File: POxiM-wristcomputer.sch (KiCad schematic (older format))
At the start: 8 parts

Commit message: schematic donish
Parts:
- removed R? (x2): R_Small, symbol Device:R_Small
- J1: renamed from J?; footprint (none) -> POxiM-uncategorised:Micro-B_Molex_105017-0001; Mfr. (none) -> Molex; Mfr. No. (none) -> 105017-0001; Mouser No. (none) -> 538-105017-0001
- J2: renamed from J?; footprint (none) -> POxiM-uncategorised:CUI_SJ-43514-SMT; Mfr. (none) -> CUI Devices; Mfr. No. (none) -> SJ-43514-SMT-TR; Mouser No. (none) -> 490-SJ-43514-SMT-TR
- gave numbers to parts that had none: 4
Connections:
- wire segments 30 -> 35
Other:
- note added: "for audio:\nmic\ngnd\nright\nleft\n"
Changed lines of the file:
@@
 F1 "Subschematics/SignalConditioning.sch" 50
 F2 "LEDDrive.IR" I L 8200 3700 50
-F3 "LEDOut.IR" O R 9850 3600 50
+F3 "LEDOut.IR" O R 9850 3800 50
 F4 "LEDDrive.Red" I L 8200 3600 50
-F5 "LEDOut.Red" O R 9850 3700 50
+F5 "LEDOut.Red" O R 9850 3900 50
 F6 "GND" I L 8200 4400 50
 F7 "PhotoDiodeInternal" O L 8200 4200 50
-F8 "PhotoDiode" I R 9850 3800 50
-F9 "+5V" I L 8200 3300 50
+F8 "PhotoDiode" I R 9850 3600 50
 $EndSheet
 $Comp
-L Connector:AudioJack4_Ground J?
+L Connector:AudioJack4_Ground J2
 U 1 1 5EBC41F5
 P 10500 3700
-F 0 "J?" H 10170 3618 50  0000 R CNN
+F 0 "J2" H 10170 3618 50  0000 R CNN
 F 1 "AudioJack4_Ground" H 10170 3527 50  0000 R CNN
-F 2 "" H 10500 3700 50  0001 C CNN
-F 3 "~" H 10500 3700 50  0001 C CNN
+F 2 "POxiM-uncategorised:CUI_SJ-43514-SMT" H 10500 3700 50  0001 C CNN
+F 3 "https://nl.mouser.com/datasheet/2/670/sj-4351x-smt-1779337.pdf" H 10500 3700 50  0001 C CNN
+F 4 "CUI Devices" H 10500 3700 50  0001 C CNN "Mfr."
+F 5 "SJ-43514-SMT-TR" H 10500 3700 50  0001 C CNN "Mfr. No."
+F 6 "490-SJ-43514-SMT-TR" H 10500 3700 50  0001 C CNN "Mouser No."
 	1    10500 3700
 	-1   0    0    -1
@@
 F6 "ADC_feedback" O R 5750 4250 50
 F7 "ADC_input" I R 5750 4150 50
-F8 "SWIM" O L 4100 3500 50
+F8 "SWIM" O L 4100 3650 50
 F9 "LED_R" O R 5750 3600 50
 F10 "LED_IR" O R 5750 3700 50
-F11 "UART1_TX" O L 4100 3600 50
+F11 "UART1_TX" O L 4100 3800 50
 $EndSheet
 $Sheet
@@
 F0 "USB interface" 50
 F1 "Subschematics/USB.sch" 50
+F2 "5V_input" I L 2150 3500 50
+F3 "5V_protected" O R 3800 3250 50
+F4 "Data+" O L 2150 3700 50
+F5 "Data-" O L 2150 3800 50
+F6 "GND" I L 2150 4450 50
+F7 "SWIM" I R 3800 3650 50
+F8 "DataTX" I R 3800 3800 50
 $EndSheet
 $Comp
-L Connector:USB_B_Micro J?
+L Connector:USB_B_Micro J1
 U 1 1 5EBC5F66
 P 950 3700
-F 0 "J?" H 1007 4167 50  0000 C CNN
+F 0 "J1" H 1007 4167 50  0000 C CNN
 F 1 "USB_B_Micro" H 1007 4076 50  0000 C CNN
-F 2 "" H 1100 3650 50  0001 C CNN
+F 2 "POxiM-uncategorised:Micro-B_Molex_105017-0001" H 1100 3650 50  0001 C CNN
 F 3 "~" H 1100 3650 50  0001 C CNN
+F 4 "Molex" H 950 3700 50  0001 C CNN "Mfr."
+F 5 "105017-0001" H 950 3700 50  0001 C CNN "Mfr. No."
+F 6 "538-105017-0001" H 950 3700 50  0001 C CNN "Mouser No."
 	1    950  3700
 	1    0    0    -1
@@
 	7550 2300 7400 2300
 $Comp
-L Mechanical:MountingHole H?
+L Mechanical:MountingHole H4
 U 1 1 5EDAD0C3
 P 1750 7400
-F 0 "H?" H 1850 7446 50  0000 L CNN
+F 0 "H4" H 1850 7446 50  0000 L CNN
 F 1 "MountingHole" H 1850 7355 50  0000 L CNN
 F 2 "MountingHole:MountingHole_2.2mm_M2_DIN965" H 1750 7400 50  0001 C CNN
 F 3 "~" H 1750 7400 50  0001 C CNN
+F 4 "~" H 1750 7400 50  0001 C CNN "Mfr."
+F 5 "~" H 1750 7400 50  0001 C CNN "Mfr. No."
+F 6 "~" H 1750 7400 50  0001 C CNN "Mouser No."
 	1    1750 7400
 	1    0    0    -1
 $EndComp
 $Comp
-L Mechanical:MountingHole H?
+L Mechanical:MountingHole H3
 U 1 1 5EDAD9CE
 P 1750 7100
-F 0 "H?" H 1850 7146 50  0000 L CNN
+F 0 "H3" H 1850 7146 50  0000 L CNN
 F 1 "MountingHole" H 1850 7055 50  0000 L CNN
 F 2 "MountingHole:MountingHole_2.2mm_M2_DIN965" H 1750 7100 50  0001 C CNN
 F 3 "~" H 1750 7100 50  0001 C CNN
+F 4 "~" H 1750 7100 50  0001 C CNN "Mfr."
+F 5 "~" H 1750 7100 50  0001 C CNN "Mfr. No."
+F 6 "~" H 1750 7100 50  0001 C CNN "Mouser No."
 	1    1750 7100
 	1    0    0    -1
 $EndComp
 $Comp
-L Mechanical:MountingHole H?
+L Mechanical:MountingHole H1
 U 1 1 5EDAE2DB
 P 900 7100
-F 0 "H?" H 1000 7146 50  0000 L CNN
+F 0 "H1" H 1000 7146 50  0000 L CNN
 F 1 "MountingHole" H 1000 7055 50  0000 L CNN
 F 2 "MountingHole:MountingHole_2.2mm_M2_DIN965" H 900 7100 50  0001 C CNN
 F 3 "~" H 900 7100 50  0001 C CNN
+F 4 "~" H 900 7100 50  0001 C CNN "Mfr."
+F 5 "~" H 900 7100 50  0001 C CNN "Mfr. No."
+F 6 "~" H 900 7100 50  0001 C CNN "Mouser No."
 	1    900  7100
 	1    0    0    -1
 $EndComp
 $Comp
-L Mechanical:MountingHole H?
+L Mechanical:MountingHole H2
 U 1 1 5EDAE92A
 P 900 7400
-F 0 "H?" H 1000 7446 50  0000 L CNN
+F 0 "H2" H 1000 7446 50  0000 L CNN
 F 1 "MountingHole" H 1000 7355 50  0000 L CNN
 F 2 "MountingHole:MountingHole_2.2mm_M2_DIN965" H 900 7400 50  0001 C CNN
 F 3 "~" H 900 7400 50  0001 C CNN
+F 4 "~" H 900 7400 50  0001 C CNN "Mfr."
+F 5 "~" H 900 7400 50  0001 C CNN "Mfr. No."
+F 6 "~" H 900 7400 50  0001 C CNN "Mouser No."
 	1    900  7400
 	1    0    0    -1
@@
 Connection ~ 950  4200
 $Comp
-L power:GND #PWR?
+L power:GND #PWR01
 U 1 1 5EDB1CEA
 P 950 4300
-F 0 "#PWR?" H 950 4050 50  0001 C CNN
+F 0 "#PWR01" H 950 4050 50  0001 C CNN
 F 1 "GND" H 955 4127 50  0000 C CNN
 F 2 "" H 950 4300 50  0001 C CNN
@@
 	1    0    0    -1
 $EndComp
-Wire Wire Line
-	1250 3500 2000 3500
 Text Label 1900 3500 2    50   ~ 0
 5V_power_input
-Wire Wire Line
-	1250 3800 1450 3800
-Wire Wire Line
-	1250 3700 1450 3700
 NoConn ~ 1250 3900
 Wire Wire Line
 	10300 3800 9850 3800
 Wire Wire Line
-	10300 3700 9850 3700
+	10300 3700 10250 3700
 Wire Wire Line
 	9850 3600 10300 3600
 Wire Wire Line
-	10300 3900 10250 3900
-Wire Wire Line
-	10250 3900 10250 4200
-Wire Wire Line
 	10500 4100 10500 4200
 Wire Wire Line
 	10500 4200 10250 4200
-Connection ~ 10250 4200
 Wire Wire Line
 	10250 4200 10250 4750
@@
 	8100 4400 8100 4800
 $Comp
-L power:GND #PWR?
+L power:GND #PWR07
 U 1 1 5EDBAF1B
 P 8100 4800
-F 0 "#PWR?" H 8100 4550 50  0001 C CNN
+F 0 "#PWR07" H 8100 4550 50  0001 C CNN
 F 1 "GND" H 8105 4627 50  0000 C CNN
 F 2 "" H 8100 4800 50  0001 C CNN
@@
 $EndComp
 $Comp
-L power:GND #PWR?
+L power:GND #PWR08
 U 1 1 5EDBAF6C
 P 10250 4750
-F 0 "#PWR?" H 10250 4500 50  0001 C CNN
+F 0 "#PWR08" H 10250 4500 50  0001 C CNN
 F 1 "GND" H 10255 4577 50  0000 C CNN
 F 2 "" H 10250 4750 50  0001 C CNN
@@
 	5750 3600 8200 3600
 Wire Wire Line
-	8200 3300 8000 3300
-Wire Wire Line
-	8000 3300 8000 3100
-$Comp
-L power:+5V #PWR?
-U 1 1 5EDBE13D
-P 8000 3100
-F 0 "#PWR?" H 8000 2950 50  0001 C CNN
-F 1 "+5V" H 8015 3273 50  0000 C CNN
-F 2 "" H 8000 3100 50  0001 C CNN
-F 3 "" H 8000 3100 50  0001 C CNN
-	1    8000 3100
-	1    0    0    -1
-$EndComp
-Wire Wire Line
 	5750 3700 8200 3700
 Wire Wire Line
@@
 	6150 4400 6150 4550
 $Comp
-L power:+5V #PWR?
+L power:+5V #PWR05
 U 1 1 5EDBFF74
 P 6150 3950
-F 0 "#PWR?" H 6150 3800 50  0001 C CNN
+F 0 "#PWR05" H 6150 3800 50  0001 C CNN
 F 1 "+5V" H 6165 4123 50  0000 C CNN
 F 2 "" H 6150 3950 50  0001 C CNN
@@
 $EndComp
 $Comp
-L power:GND #PWR?
+L power:GND #PWR06
 U 1 1 5EDC0E1F
 P 6150 4550
-F 0 "#PWR?" H 6150 4300 50  0001 C CNN
+F 0 "#PWR06" H 6150 4300 50  0001 C CNN
 F 1 "GND" H 6155 4377 50  0000 C CNN
 F 2 "" H 6150 4550 50  0001 C CNN
@@
 	1    0    0    -1
 $EndComp
-$Comp
-L Device:R_Small R?
-U 1 1 5EDC2FF6
-P 1550 3700
-F 0 "R?" V 1746 3700 50  0000 C CNN
-F 1 "R_Small" V 1655 3700 50  0000 C CNN
-F 2 "" H 1550 3700 50  0001 C CNN
-F 3 "~" H 1550 3700 50  0001 C CNN
-	1    1550 3700
-	0    -1   -1   0
-$EndComp
-Wire Wire Line
-	1650 3700 2000 3700
-$Comp
-L Device:R_Small R?
-U 1 1 5EDC4868
-P 1550 3800
-F 0 "R?" V 1746 3800 50  0000 C CNN
-F 1 "R_Small" V 1655 3800 50  0000 C CNN
-F 2 "" H 1550 3800 50  0001 C CNN
-F 3 "~" H 1550 3800 50  0001 C CNN
-	1    1550 3800
-	0    -1   -1   0
-$EndComp
-Wire Wire Line
-	1650 3800 2000 3800
+Wire Wire Line
+	4100 3650 3800 3650
+Wire Wire Line
+	4100 3800 3800 3800
+Wire Wire Line
+	3800 3250 3950 3250
+Wire Wire Line
+	3950 3250 3950 2700
+Connection ~ 3950 3250
+Wire Wire Line
+	3950 3250 4100 3250
+$Comp
+L power:+5V #PWR04
+U 1 1 5EBC7CAA
+P 3950 2700
+F 0 "#PWR04" H 3950 2550 50  0001 C CNN
+F 1 "+5V" H 3965 2873 50  0000 C CNN
+F 2 "" H 3950 2700 50  0001 C CNN
+F 3 "" H 3950 2700 50  0001 C CNN
+	1    3950 2700
+	1    0    0    -1
+$EndComp
+$Comp
+L power:GND #PWR02
+U 1 1 5EBC7E84
+P 1950 4600
+F 0 "#PWR02" H 1950 4350 50  0001 C CNN
+F 1 "GND" H 1955 4427 50  0000 C CNN
+F 2 "" H 1950 4600 50  0001 C CNN
+F 3 "" H 1950 4600 50  0001 C CNN
+	1    1950 4600
+	1    0    0    -1
+$EndComp
+Wire Wire Line
+	2150 4450 1950 4450
+Wire Wire Line
+	1950 4450 1950 4600
+Wire Wire Line
+	1250 3500 2150 3500
+Wire Wire Line
+	1250 3800 2150 3800
+Wire Wire Line
+	1250 3700 2150 3700
+$Comp
+L power:GND #PWR03
+U 1 1 5EBE7B4C
+P 3900 4600
+F 0 "#PWR03" H 3900 4350 50  0001 C CNN
+F 1 "GND" H 3905 4427 50  0000 C CNN
+F 2 "" H 3900 4600 50  0001 C CNN
+F 3 "" H 3900 4600 50  0001 C CNN
+	1    3900 4600
+	1    0    0    -1
+$EndComp
+Wire Wire Line
+	4100 4450 3900 4450
+Wire Wire Line
+	3900 4450 3900 4600
+Wire Wire Line
+	10250 3700 10250 4200
+Connection ~ 10250 4200
+Wire Wire Line
+	10300 3900 9850 3900
+Text Notes 10400 3400 0    50   ~ 0
+for audio:\nmic\ngnd\nright\nleft\n
 $EndSCHEMATC

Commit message: looks real
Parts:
- removed H3, H4: MountingHole, MountingHole:MountingHole_2.2mm_M2_DIN965, symbol Mechanical:MountingHole
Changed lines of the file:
@@
 EESchema Schematic File Version 4
-LIBS:POxiM-wristcomputer-cache
-EELAYER 29 0
+EELAYER 30 0
 EELAYER END
 $Descr A4 11693 8268
@@
 	7550 2300 7400 2300
 $Comp
-L Mechanical:MountingHole H4
-U 1 1 5EDAD0C3
-P 1750 7400
-F 0 "H4" H 1850 7446 50  0000 L CNN
-F 1 "MountingHole" H 1850 7355 50  0000 L CNN
-F 2 "MountingHole:MountingHole_2.2mm_M2_DIN965" H 1750 7400 50  0001 C CNN
-F 3 "~" H 1750 7400 50  0001 C CNN
-F 4 "~" H 1750 7400 50  0001 C CNN "Mfr."
-F 5 "~" H 1750 7400 50  0001 C CNN "Mfr. No."
-F 6 "~" H 1750 7400 50  0001 C CNN "Mouser No."
-	1    1750 7400
-	1    0    0    -1
-$EndComp
-$Comp
-L Mechanical:MountingHole H3
-U 1 1 5EDAD9CE
-P 1750 7100
-F 0 "H3" H 1850 7146 50  0000 L CNN
-F 1 "MountingHole" H 1850 7055 50  0000 L CNN
-F 2 "MountingHole:MountingHole_2.2mm_M2_DIN965" H 1750 7100 50  0001 C CNN
-F 3 "~" H 1750 7100 50  0001 C CNN
-F 4 "~" H 1750 7100 50  0001 C CNN "Mfr."
-F 5 "~" H 1750 7100 50  0001 C CNN "Mfr. No."
-F 6 "~" H 1750 7100 50  0001 C CNN "Mouser No."
-	1    1750 7100
-	1    0    0    -1
-$EndComp
-$Comp
 L Mechanical:MountingHole H1

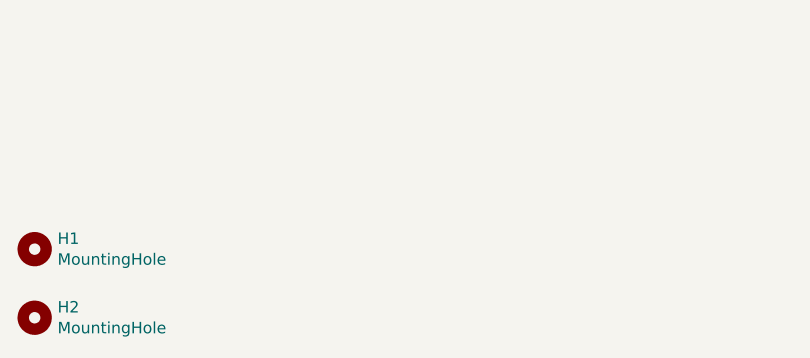
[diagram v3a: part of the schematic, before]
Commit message: Refactor based on feedback from Daniel
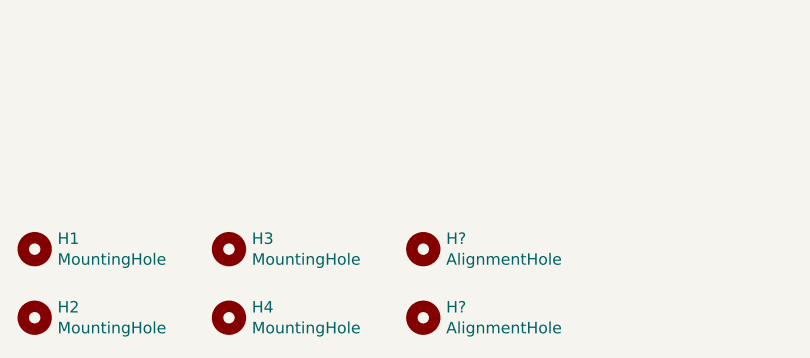
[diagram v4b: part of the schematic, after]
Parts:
- added H3, H4: MountingHole, MountingHole:MountingHole_2.2mm_M2_DIN965, symbol Mechanical:MountingHole
- added H? (x2): AlignmentHole, MountingHole:MountingHole_2.2mm_M2_DIN965, symbol Mechanical:MountingHole
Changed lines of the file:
@@
 EESchema Schematic File Version 4
-EELAYER 30 0
+LIBS:POxiM-wristcomputer-cache
+EELAYER 29 0
 EELAYER END
 $Descr A4 11693 8268
@@
 Text Notes 10400 3400 0    50   ~ 0
 for audio:\nmic\ngnd\nright\nleft\n
+$Comp
+L Mechanical:MountingHole H3
+U 1 1 5EBE9DDE
+P 1750 7100
+F 0 "H3" H 1850 7146 50  0000 L CNN
+F 1 "MountingHole" H 1850 7055 50  0000 L CNN
+F 2 "MountingHole:MountingHole_2.2mm_M2_DIN965" H 1750 7100 50  0001 C CNN
+F 3 "~" H 1750 7100 50  0001 C CNN
+F 4 "~" H 1750 7100 50  0001 C CNN "Mfr."
+F 5 "~" H 1750 7100 50  0001 C CNN "Mfr. No."
+F 6 "~" H 1750 7100 50  0001 C CNN "Mouser No."
+	1    1750 7100
+	1    0    0    -1
+$EndComp
+$Comp
+L Mechanical:MountingHole H4
+U 1 1 5EBE9DE7
+P 1750 7400
+F 0 "H4" H 1850 7446 50  0000 L CNN
+F 1 "MountingHole" H 1850 7355 50  0000 L CNN
+F 2 "MountingHole:MountingHole_2.2mm_M2_DIN965" H 1750 7400 50  0001 C CNN
+F 3 "~" H 1750 7400 50  0001 C CNN
+F 4 "~" H 1750 7400 50  0001 C CNN "Mfr."
+F 5 "~" H 1750 7400 50  0001 C CNN "Mfr. No."
+F 6 "~" H 1750 7400 50  0001 C CNN "Mouser No."
+	1    1750 7400
+	1    0    0    -1
+$EndComp
+$Comp
+L Mechanical:MountingHole H?
+U 1 1 5EC0DFF9
+P 2600 7100
+F 0 "H?" H 2700 7146 50  0000 L CNN
+F 1 "AlignmentHole" H 2700 7055 50  0000 L CNN
+F 2 "MountingHole:MountingHole_2.2mm_M2_DIN965" H 2600 7100 50  0001 C CNN
+F 3 "~" H 2600 7100 50  0001 C CNN
+F 4 "~" H 2600 7100 50  0001 C CNN "Mfr."
+F 5 "~" H 2600 7100 50  0001 C CNN "Mfr. No."
+F 6 "~" H 2600 7100 50  0001 C CNN "Mouser No."
+	1    2600 7100
+	1    0    0    -1
+$EndComp
+$Comp
+L Mechanical:MountingHole H?
+U 1 1 5EC0E002
+P 2600 7400
+F 0 "H?" H 2700 7446 50  0000 L CNN
+F 1 "AlignmentHole" H 2700 7355 50  0000 L CNN
+F 2 "MountingHole:MountingHole_2.2mm_M2_DIN965" H 2600 7400 50  0001 C CNN
+F 3 "~" H 2600 7400 50  0001 C CNN
+F 4 "~" H 2600 7400 50  0001 C CNN "Mfr."
+F 5 "~" H 2600 7400 50  0001 C CNN "Mfr. No."
+F 6 "~" H 2600 7400 50  0001 C CNN "Mouser No."
+	1    2600 7400
+	1    0    0    -1
+$EndComp
 $EndSCHEMATC

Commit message: Finish display tester board Rev A
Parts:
- added D10, D11, D12, D13, D14, D15, D16, D17, D18, D19, D20, D21, D22, D23, D24, D25, D26, D27, D28, D29, D30, D7, D8, D9: LED, LED_SMD:LED_0805_2012Metric_Castellated, symbol Device:LED
- added J14, JP16, JP18, JP20, JP27, JP28, JP29, JP30, JP31, JP8: Jumper_NO_Small, POxiM-uncategorised:SolderJumper-2_P1.3mm_Open_RoundedPad1.0x1.5mm, symbol Device:Jumper_NO_Small
- added JP10, JP11, JP12, JP13, JP15, JP17, JP19, JP21, JP22, JP23, JP24, JP25, JP26, JP9: Jumper_NC_Small, POxiM-uncategorised:SolderJumper-2_P1.3mm_SolderBridged_RoundedPad1.0x1.5mm, symbol Device:Jumper_NC_Small
- added R10, R11, R12, R13, R14, R15, R16, R17, R18, R19, R20, R21, R22, R23, R24, R25, R26, R27, R28, R29, R30, R7, R8, R9: 4.7kΩ, Resistor_SMD:R_0805_2012Metric_Pad1.15x1.40mm_HandSolder, symbol Device:R_Small
- gave numbers to parts that had none: 2
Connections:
- net 5V_power_input is gone; now on net +5V: J1.1 (VBUS)
- net +5V: now also J14.1, JP10.1, JP11.1, JP12.1, JP13.1, JP15.1, JP16.1, JP17.1, JP18.1, JP19.1, JP20.1, JP21.1, JP22.1, JP23.1, JP24.1, JP25.1, JP26.1, JP27.1, JP28.1, JP29.1, JP30.1, JP31.1, JP8.1, JP9.1
- net GND: now also D10.1 (K), D11.1 (K), D12.1 (K), D13.1 (K), D14.1 (K), D15.1 (K), D16.1 (K), D17.1 (K), D18.1 (K), D19.1 (K), D20.1 (K), D21.1 (K), D22.1 (K), D23.1 (K), D24.1 (K), D25.1 (K), D26.1 (K), D27.1 (K), D28.1 (K), D29.1 (K), D30.1 (K), D7.1 (K), D8.1 (K), D9.1 (K)
- net Signal conditioning/LEDOut.IR: no longer names the net of J2.R1
- net Signal conditioning/LEDOut.Red: no longer names the net of J2.T
- net Signal conditioning/PhotoDiode: no longer names the net of J2.S
- net USB interface/Data+: no longer names the net of J1.3 (D+)
- net USB interface/Data-: no longer names the net of J1.2 (D-)
- new net: D8.2 (A), R8.2
- new net: D10.2 (A), R10.2
- new net: D12.2 (A), R12.2
- new net: D14.2 (A), R14.2
- new net: D16.2 (A), R16.2
- new net: D18.2 (A), R18.2
- new net: D20.2 (A), R20.2
- new net: JP9.2, R8.1
- new net: JP11.2, R10.1
- new net: JP13.2, R12.1
- new net: JP15.2, R14.1
- new net: JP17.2, R16.1
- new net: JP19.2, R18.1
- new net: JP21.2, R20.1
- new net: D7.2 (A), R7.2
- new net: D9.2 (A), R9.2
- new net: D11.2 (A), R11.2
- new net: D13.2 (A), R13.2
- new net: D15.2 (A), R15.2
- new net: D17.2 (A), R17.2
- new net: D19.2 (A), R19.2
- new net: JP8.2, R7.1
- new net: JP10.2, R9.1
- new net: JP12.2, R11.1
- new net: J14.2, R13.1
- new net: JP16.2, R15.1
- new net: JP18.2, R17.1
- new net: JP20.2, R19.1
- new net: D21.2 (A), R21.2
- new net: D23.2 (A), R23.2
- new net: D25.2 (A), R25.2
- new net: D27.2 (A), R27.2
- new net: D28.2 (A), R28.2
- new net: D29.2 (A), R29.2
- new net: D30.2 (A), R30.2
- new net: JP22.2, R21.1
- new net: JP24.2, R23.1
- new net: JP26.2, R25.1
- new net: JP28.2, R27.1
- new net: JP29.2, R28.1
- new net: JP30.2, R29.1
- new net: JP31.2, R30.1
- new net: D22.2 (A), R22.2
- new net: D24.2 (A), R24.2
- new net: D26.2 (A), R26.2
- new net: JP23.2, R22.1
- new net: JP25.2, R24.1
- new net: JP27.2, R26.1
- no-connect marks 1 -> 6
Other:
- note added: "Digit 0"
- note added: "Digit 1"
- note added: "Digit 2"
- note added: "Digit AUX"
- moved on the sheet: J2

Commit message: Finish works-as prototype design
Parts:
- removed D10, D11, D12, D13, D14, D15, D16, D17, D18, D19, D20, D21, D22, D23, D24, D25, D26, D27, D28, D29, D30, D7, D8, D9: LED, LED_SMD:LED_0805_2012Metric_Castellated, symbol Device:LED
- removed J14, JP16, JP18, JP20, JP27, JP28, JP29, JP30, JP31, JP8: Jumper_NO_Small, POxiM-uncategorised:SolderJumper-2_P1.3mm_Open_RoundedPad1.0x1.5mm, symbol Device:Jumper_NO_Small
- removed JP10, JP11, JP12, JP13, JP15, JP17, JP19, JP21, JP22, JP23, JP24, JP25, JP26, JP9: Jumper_NC_Small, POxiM-uncategorised:SolderJumper-2_P1.3mm_SolderBridged_RoundedPad1.0x1.5mm, symbol Device:Jumper_NC_Small
- removed R10, R11, R12, R13, R14, R15, R16, R17, R18, R19, R20, R21, R22, R23, R24, R25, R26, R27, R28, R29, R30, R7, R8, R9: 4.7kΩ, Resistor_SMD:R_0805_2012Metric_Pad1.15x1.40mm_HandSolder, symbol Device:R_Small
- added J10, J9: Mains_noise_conn, Connector_Coaxial:SMA_Molex_73251-2200_Horizontal, symbol Connector:Conn_Coaxial
- added J11: AudioJack4_Ground, POxiM-uncategorised:CUI_SJ-43514-SMT, symbol Connector:AudioJack4_Ground
- added J3, J8: USB_B_Micro, POxiM-uncategorised:Micro-B_Molex_105017-0001, symbol Connector:USB_B_Micro
- added J4, J5: USB_A, POxiM-uncategorised:USBA_87583-2010RLF, symbol Connector:USB_A
- added J6: Uart Out, Connector_PinHeader_2.54mm:PinHeader_1x02_P2.54mm_Vertical, symbol Connector:Conn_01x02_Male
- added J7: Programming Header, Connector_PinHeader_2.54mm:PinHeader_2x05_P2.54mm_Vertical, symbol Connector:Conn_01x10_Male
- added MB1, MB2, MB3, MB4, MB5, MB6, MB7, MB8: Bumpon, POxiM-uncategorised:Bumpon-SJ-5007BK, symbol POxiM-mechanical:Bumpon
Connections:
- net +5V: no longer J1.1 (VBUS)
- net Signal conditioning/LEDOut.IR: now reaches J2.R1
- net Signal conditioning/PhotoDiode: now reaches J2.S
- net Signal conditioning/LEDOut.Red: now reaches J2.T
- net USB interface/Data-: now reaches J1.2 (D-)
- net USB interface/Data+: now reaches J1.3 (D+)
- new net: J3.1 (VBUS), J4.1 (VBUS), J5.1 (VBUS)
- new net: J4.2 (D-), J5.2 (D-), J6.1 (Pin_1)
- new net: J4.3 (D+), J5.3 (D+), J7.5 (Pin_5)
- new net: J3.5 (GND), J3.6 (Shield), J4.4 (GND), J4.5 (Shield), J5.4 (GND), J5.5 (Shield), J6.2 (Pin_2), J7.3 (Pin_3), J7.4 (Pin_4)
- new net 5V_power_input: J1.1 (VBUS)
- new net Testing finger board/5V: J8.1 (VBUS)
- new net Testing finger board/GND: J10.2 (Ext), J11.G, J11.R2, J8.5 (GND), J8.6 (Shield), J9.2 (Ext)
- new net Testing finger board/Heartbeat: J10.1 (In)
- new net Testing finger board/LED_IR: J11.R1
- new net Testing finger board/LED_R: J11.T
- new net Testing finger board/Mains_noise: J9.1 (In)
- new net Testing finger board/Photodiode: J11.S
- no-connect marks 6 -> 11
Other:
- note added: "Finger pretender board"
- note added: "Programming board"
- note removed: "Digit 0"
- note removed: "Digit 1"
- note removed: "Digit 2"
- note removed: "Digit AUX"
- moved on the sheet: H1, H2, H3, H4, H5, H6, J1, J2
